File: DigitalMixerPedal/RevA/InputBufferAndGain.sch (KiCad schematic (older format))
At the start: 7 parts, among them U2 TL072

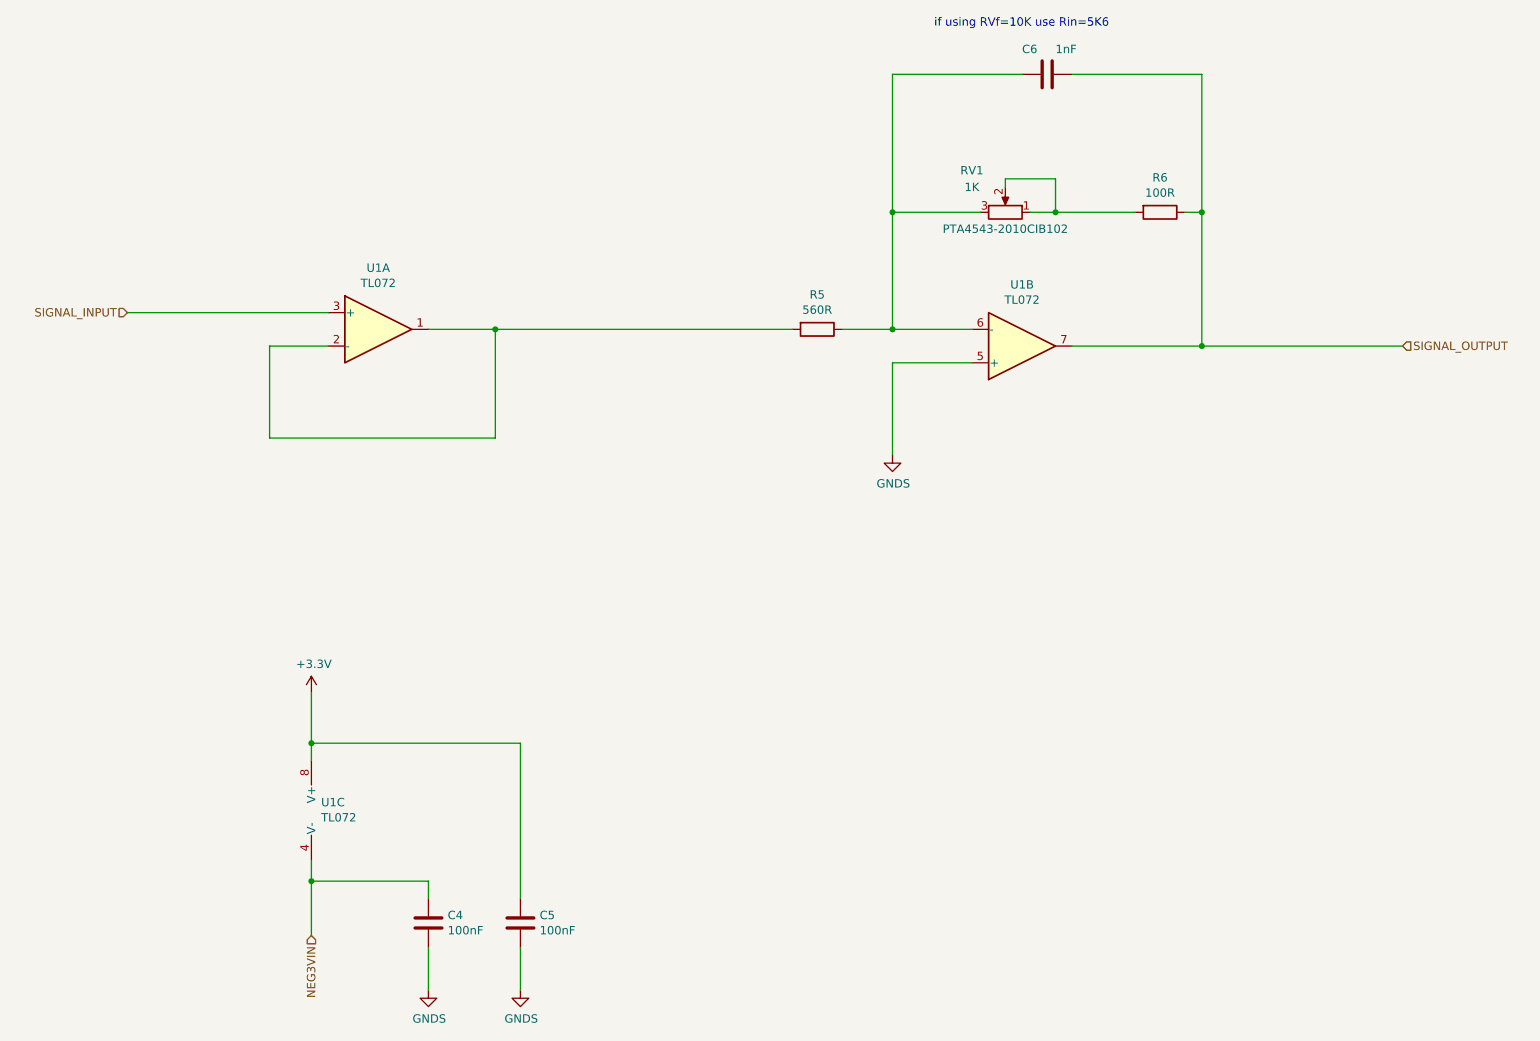
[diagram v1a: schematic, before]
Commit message: updated hw
- added testpoints
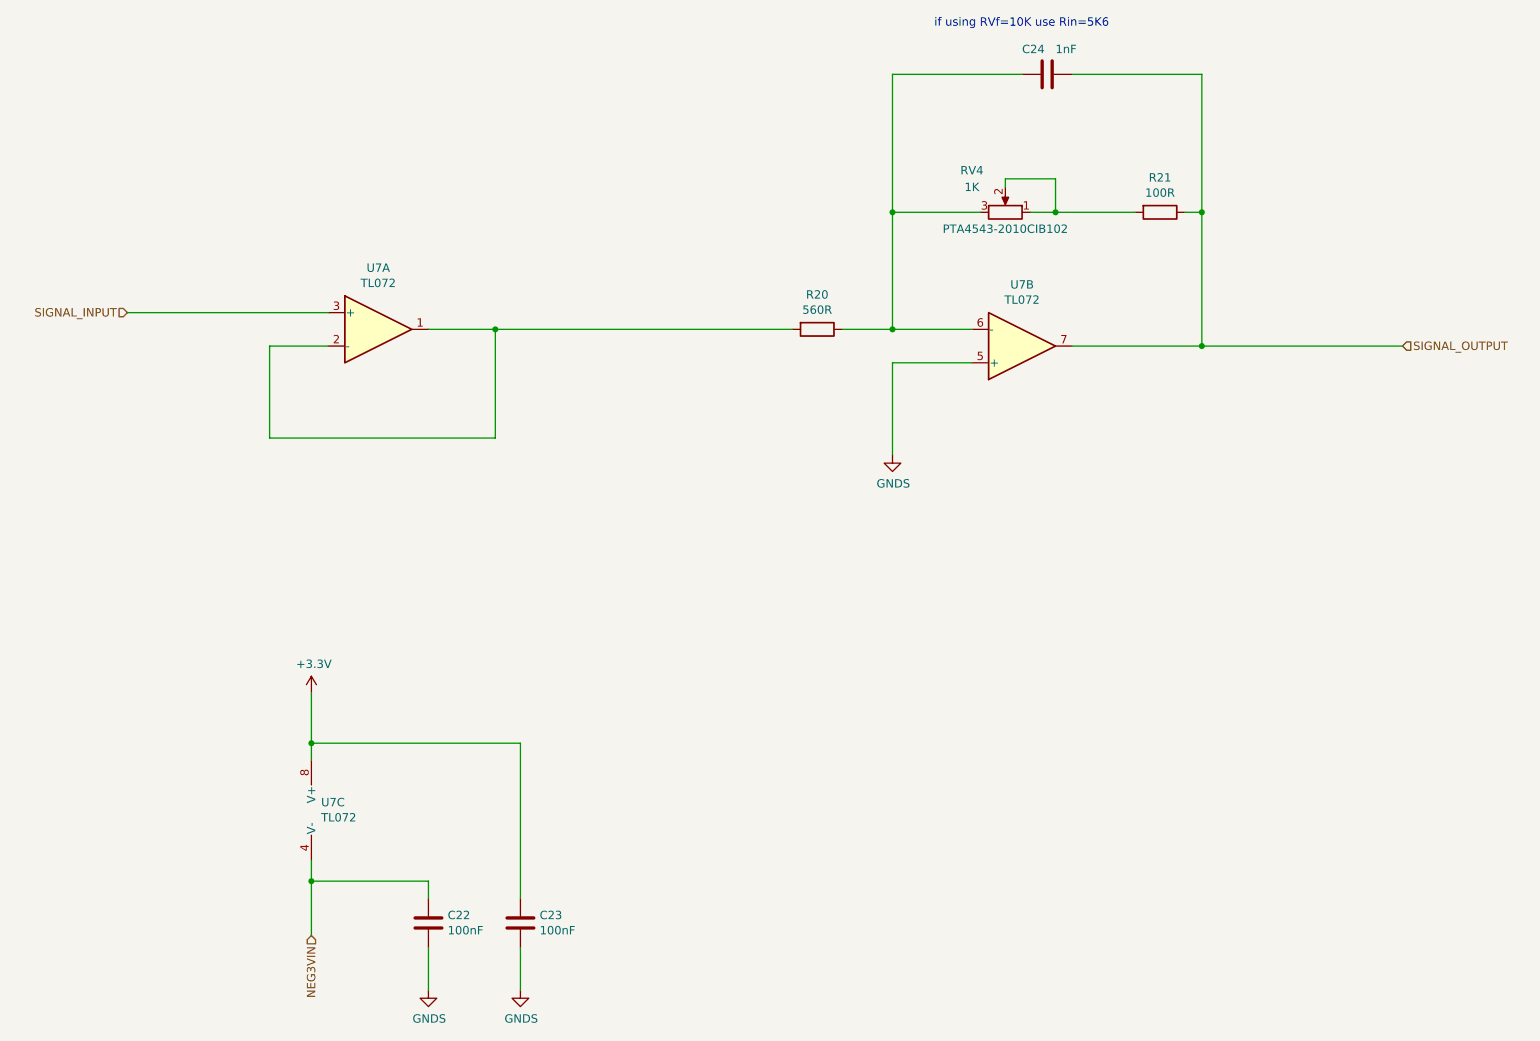
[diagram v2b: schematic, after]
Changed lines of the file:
@@
 AR Path="/5F5BB12C/5F59292E" Ref="R15"  Part="1"
 AR Path="/5F5BCC25/5F59292E" Ref="R20"  Part="1"
-F 0 "R5" V 6018 2875 50  0000 C CNN
+F 0 "R20" V 6018 2875 50  0000 C CNN
 F 1 "560R" V 6109 2875 50  0000 C CNN
 F 2 "Resistor_SMD:R_0805_2012Metric_Pad1.15x1.40mm_HandSolder" V 6155 2875 50  0001 C CNN
@@
 AR Path="/5F5BB12C/5F59293F" Ref="RV3"  Part="1"
 AR Path="/5F5BCC25/5F59293F" Ref="RV4"  Part="1"
-F 0 "RV1" V 7600 1975 50  0000 C CNN
+F 0 "RV4" V 7600 1975 50  0000 C CNN
 F 1 "1K" V 7500 1975 50  0000 C CNN
 F 2 "Bourn_PTA_Slider:Slider_PTA4543_60MM" H 7350 2175 50  0001 C CNN
@@
 AR Path="/5F5BB12C/5F592956" Ref="R16"  Part="1"
 AR Path="/5F5BCC25/5F592956" Ref="R21"  Part="1"
-F 0 "R6" V 8068 2175 50  0000 C CNN
+F 0 "R21" V 8068 2175 50  0000 C CNN
 F 1 "100R" V 8159 2175 50  0000 C CNN
 F 2 "Resistor_SMD:R_0805_2012Metric_Pad1.15x1.40mm_HandSolder" V 8205 2175 50  0001 C CNN
@@
 AR Path="/5F5BB12C/5F59295D" Ref="C18"  Part="1"
 AR Path="/5F5BCC25/5F59295D" Ref="C24"  Part="1"
-F 0 "C6" V 7450 1200 50  0000 L CNN
+F 0 "C24" V 7450 1200 50  0000 L CNN
 F 1 "1nF" V 7450 1400 50  0000 L CNN
 F 2 "Capacitor_SMD:C_0805_2012Metric_Pad1.15x1.40mm_HandSolder" H 7638 1200 50  0001 C CNN
@@
 AR Path="/5F5BB12C/5F59AE7C" Ref="U5"  Part="1"
 AR Path="/5F5BCC25/5F59AE7C" Ref="U7"  Part="1"
-F 0 "U1" H 3600 3242 50  0000 C CNN
+F 0 "U7" H 3600 3242 50  0000 C CNN
 F 1 "TL072" H 3600 3151 50  0000 C CNN
 F 2 "Package_SO:SOIC-8_3.9x4.9mm_P1.27mm" H 3600 2875 50  0001 C CNN
@@
 AR Path="/5F5BB12C/5F59C9C2" Ref="U5"  Part="2"
 AR Path="/5F5BCC25/5F59C9C2" Ref="U7"  Part="2"
-F 0 "U1" H 7450 2608 50  0000 C CNN
+F 0 "U7" H 7450 2608 50  0000 C CNN
 F 1 "TL072" H 7450 2699 50  0000 C CNN
 F 2 "Package_SO:SOIC-8_3.9x4.9mm_P1.27mm" H 7450 2975 50  0001 C CNN
@@
 AR Path="/5F5BB12C/5F59E5A5" Ref="U5"  Part="3"
 AR Path="/5F5BCC25/5F59E5A5" Ref="U7"  Part="3"
-F 0 "U1" H 3258 5796 50  0000 L CNN
+F 0 "U7" H 3258 5796 50  0000 L CNN
 F 1 "TL072" H 3258 5705 50  0000 L CNN
 F 2 "Package_SO:SOIC-8_3.9x4.9mm_P1.27mm" H 3300 5750 50  0001 C CNN
@@
 AR Path="/5F5BB12C/5F5D3555" Ref="C16"  Part="1"
 AR Path="/5F5BCC25/5F5D3555" Ref="C22"  Part="1"
-F 0 "C4" H 4015 6471 50  0000 L CNN
+F 0 "C22" H 4015 6471 50  0000 L CNN
 F 1 "100nF" H 4015 6380 50  0000 L CNN
 F 2 "Capacitor_SMD:C_0805_2012Metric_Pad1.15x1.40mm_HandSolder" H 3938 6275 50  0001 C CNN
@@
 AR Path="/5F5BB12C/5F5D446F" Ref="C17"  Part="1"
 AR Path="/5F5BCC25/5F5D446F" Ref="C23"  Part="1"
-F 0 "C5" H 4565 6471 50  0000 L CNN
+F 0 "C23" H 4565 6471 50  0000 L CNN
 F 1 "100nF" H 4565 6380 50  0000 L CNN
 F 2 "Capacitor_SMD:C_0805_2012Metric_Pad1.15x1.40mm_HandSolder" H 4488 6275 50  0001 C CNN
